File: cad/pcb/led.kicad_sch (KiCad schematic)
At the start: 0 parts

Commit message: finish overview schematic page
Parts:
- added IC?: PI4IOE5V96224ZLEX, QFN40P300X600X80-33N, symbol PI4IOE5V96224ZLEX:PI4IOE5V96224ZLEX
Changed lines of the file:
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@@
     (comment 4 "Simon Brenninger")
   )
+  (symbol (lib_id "PI4IOE5V96224ZLEX:PI4IOE5V96224ZLEX") (at 59.69 52.07 0) (unit 1)
+    (in_bom yes) (on_board yes) (fields_autoplaced)
+    (property "Reference" "IC?" (id 0) (at 82.0294 92.71 0)
+      (effects (font (size 1.27 1.27)) (justify left))
+    )
+    (property "Value" "PI4IOE5V96224ZLEX" (id 1) (at 82.0294 95.25 0)
+      (effects (font (size 1.27 1.27)) (justify left))
+    )
+    (property "Footprint" "QFN40P300X600X80-33N" (id 2) (at 88.9 41.91 0)
+      (effects (font (size 1.27 1.27)) (justify left) hide)
+    )
+    (property "Datasheet" "https://www.diodes.com/assets/Datasheets/PI4IOE5V96224.pdf" (id 3) (at 88.9 44.45 0)
+      (effects (font (size 1.27 1.27)) (justify left) hide)
+    )
+    (property "Description" "Interface - I/O Expanders 24-bit I2C-bus I/O Expander" (id 4) (at 88.9 46.99 0)
+      (effects (font (size 1.27 1.27)) (justify left) hide)
+    )
+    (property "Height" "0.8" (id 5) (at 88.9 49.53 0)
+      (effects (font (size 1.27 1.27)) (justify left) hide)
+    )
+    (property "Mouser Part Number" "729-I4IOE5V96224ZLEX" (id 6) (at 88.9 52.07 0)
+      (effects (font (size 1.27 1.27)) (justify left) hide)
+    )
+    (property "Mouser Price/Stock" "https://www.mouser.co.uk/ProductDetail/Diodes-Incorporated/PI4IOE5V96224ZLEX?qs=0lQeLiL1qybZKU%252B6WN8aKg%3D%3D" (id 7) (at 88.9 54.61 0)
+      (effects (font (size 1.27 1.27)) (justify left) hide)
+    )
+    (property "Manufacturer_Name" "Diodes Inc." (id 8) (at 88.9 57.15 0)
+      (effects (font (size 1.27 1.27)) (justify left) hide)
+    )
+    (property "Manufacturer_Part_Number" "PI4IOE5V96224ZLEX" (id 9) (at 88.9 59.69 0)
+      (effects (font (size 1.27 1.27)) (justify left) hide)
+    )
+    (pin "1")
+    (pin "10")
+    (pin "11")
+    (pin "12")
+    (pin "13")
+    (pin "14")
+    (pin "15")
+    (pin "16")
+    (pin "17")
+    (pin "18")
+    (pin "19")
+    (pin "2")
+    (pin "20")
+    (pin "21")
+    (pin "22")
+    (pin "23")
+    (pin "24")
+    (pin "25")
+    (pin "26")
+    (pin "27")
+    (pin "28")
+    (pin "29")
+    (pin "3")
+    (pin "30")
+    (pin "31")
+    (pin "32")
+    (pin "33")
+    (pin "4")
+    (pin "5")
+    (pin "6")
+    (pin "7")
+    (pin "8")
+    (pin "9")
+  )
 )

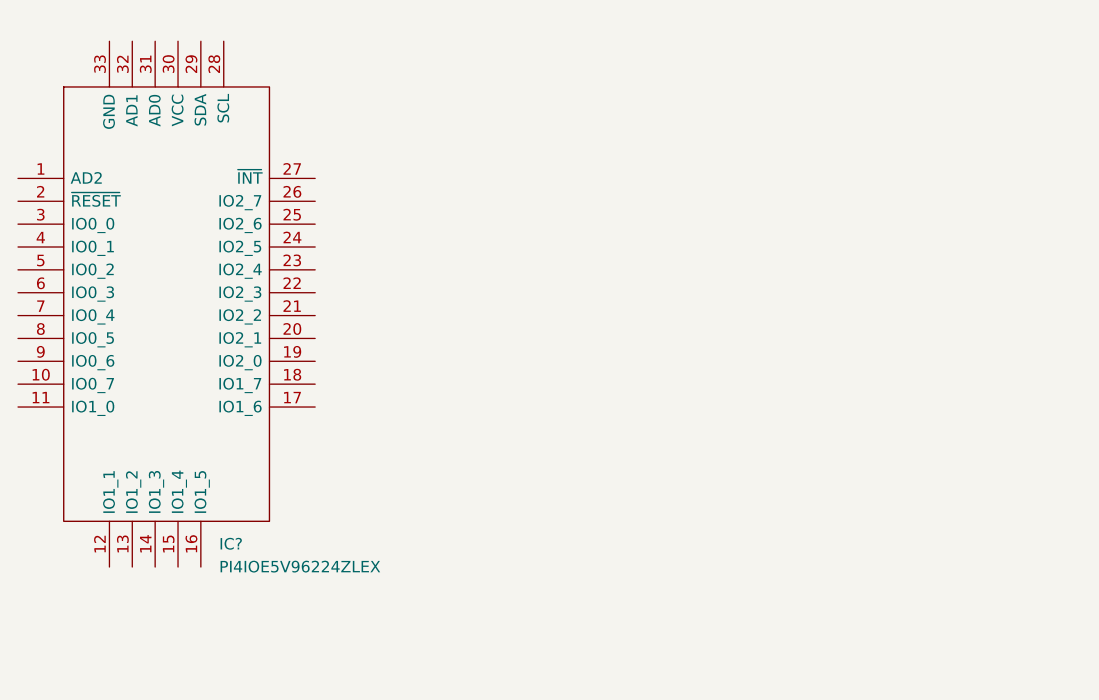
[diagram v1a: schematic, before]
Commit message: finish mcu connections
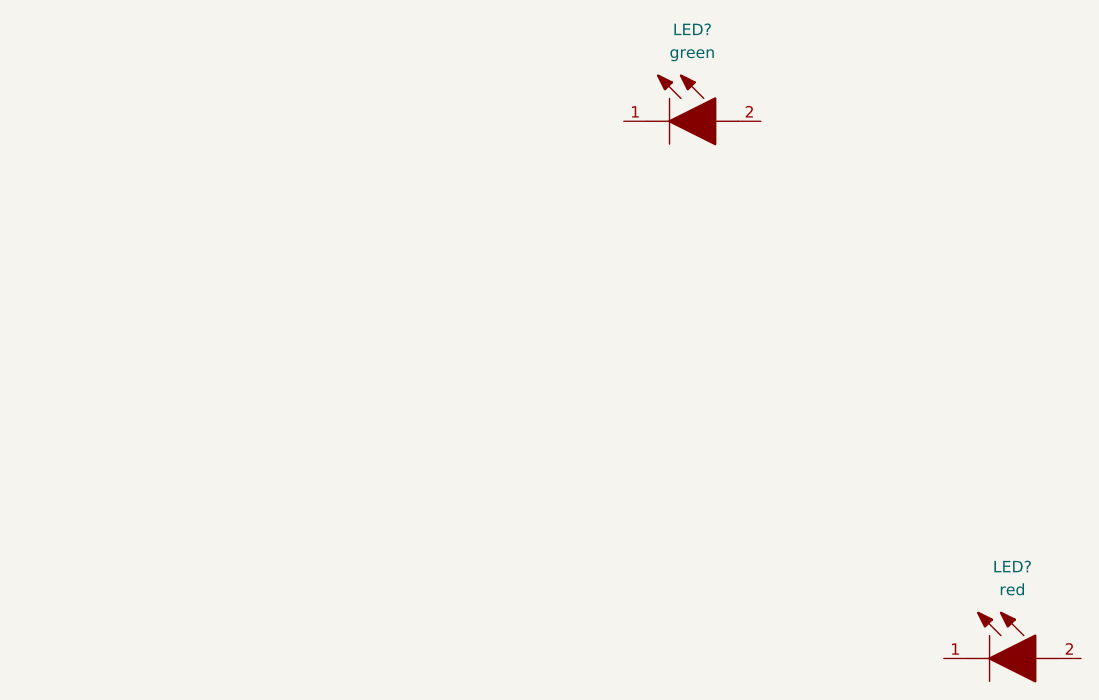
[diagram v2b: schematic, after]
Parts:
- removed IC?: PI4IOE5V96224ZLEX, QFN40P300X600X80-33N, symbol PI4IOE5V96224ZLEX:PI4IOE5V96224ZLEX
- added LED?: red, LEDC1608X80N, symbol LED red:150060SS75000
- added LED?: green, LEDM2012X80N, symbol LED green:150080GS75000
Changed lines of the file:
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@@
     (comment 4 "Simon Brenninger")
   )
-  (symbol (lib_id "PI4IOE5V96224ZLEX:PI4IOE5V96224ZLEX") (at 59.69 52.07 0) (unit 1)
+  (symbol (lib_id "LED red:150060SS75000") (at 162.56 105.41 0) (unit 1)
     (in_bom yes) (on_board yes) (fields_autoplaced)
-    (property "Reference" "IC?" (id 0) (at 82.0294 92.71 0)
-      (effects (font (size 1.27 1.27)) (justify left))
+    (property "Reference" "LED?" (id 0) (at 170.18 95.25 0))
+    (property "Value" "red" (id 1) (at 170.18 97.79 0))
+    (property "Footprint" "LEDC1608X80N" (id 2) (at 175.26 101.6 0)
+      (effects (font (size 1.27 1.27)) (justify left bottom) hide)
     )
-    (property "Value" "PI4IOE5V96224ZLEX" (id 1) (at 82.0294 95.25 0)
-      (effects (font (size 1.27 1.27)) (justify left))
+    (property "Datasheet" "" (id 3) (at 175.26 104.14 0)
+      (effects (font (size 1.27 1.27)) (justify left bottom) hide)
     )
-    (property "Footprint" "QFN40P300X600X80-33N" (id 2) (at 88.9 41.91 0)
-      (effects (font (size 1.27 1.27)) (justify left) hide)
+    (property "Description" "LED,Wurth Elektronik,150060SS75000 Wurth Elektronik 150060SS75000, WL-SMCW Series Red LED, 630 nm, 1608 (0603) Clear, Rectangle Lens SMD Package" (id 4) (at 175.26 106.68 0)
+      (effects (font (size 1.27 1.27)) (justify left bottom) hide)
     )
-    (property "Datasheet" "https://www.diodes.com/assets/Datasheets/PI4IOE5V96224.pdf" (id 3) (at 88.9 44.45 0)
-      (effects (font (size 1.27 1.27)) (justify left) hide)
+    (property "Height" "0.8" (id 5) (at 175.26 109.22 0)
+      (effects (font (size 1.27 1.27)) (justify left bottom) hide)
     )
-    (property "Description" "Interface - I/O Expanders 24-bit I2C-bus I/O Expander" (id 4) (at 88.9 46.99 0)
-      (effects (font (size 1.27 1.27)) (justify left) hide)
+    (property "Mouser Part Number" "710-150060SS75000" (id 6) (at 175.26 111.76 0)
+      (effects (font (size 1.27 1.27)) (justify left bottom) hide)
     )
-    (property "Height" "0.8" (id 5) (at 88.9 49.53 0)
-      (effects (font (size 1.27 1.27)) (justify left) hide)
+    (property "Mouser Price/Stock" "https://www.mouser.co.uk/ProductDetail/Wurth-Elektronik/150060SS75000?qs=LlUlMxKIyB0oQaxwspeTEA%3D%3D" (id 7) (at 175.26 114.3 0)
+      (effects (font (size 1.27 1.27)) (justify left bottom) hide)
     )
-    (property "Mouser Part Number" "729-I4IOE5V96224ZLEX" (id 6) (at 88.9 52.07 0)
-      (effects (font (size 1.27 1.27)) (justify left) hide)
+    (property "Manufacturer_Name" "Wurth Elektronik" (id 8) (at 175.26 116.84 0)
+      (effects (font (size 1.27 1.27)) (justify left bottom) hide)
     )
-    (property "Mouser Price/Stock" "https://www.mouser.co.uk/ProductDetail/Diodes-Incorporated/PI4IOE5V96224ZLEX?qs=0lQeLiL1qybZKU%252B6WN8aKg%3D%3D" (id 7) (at 88.9 54.61 0)
-      (effects (font (size 1.27 1.27)) (justify left) hide)
-    )
-    (property "Manufacturer_Name" "Diodes Inc." (id 8) (at 88.9 57.15 0)
-      (effects (font (size 1.27 1.27)) (justify left) hide)
-    )
-    (property "Manufacturer_Part_Number" "PI4IOE5V96224ZLEX" (id 9) (at 88.9 59.69 0)
-      (effects (font (size 1.27 1.27)) (justify left) hide)
+    (property "Manufacturer_Part_Number" "150060SS75000" (id 9) (at 175.26 119.38 0)
+      (effects (font (size 1.27 1.27)) (justify left bottom) hide)
     )
     (pin "1")
-    (pin "10")
-    (pin "11")
-    (pin "12")
-    (pin "13")
-    (pin "14")
-    (pin "15")
-    (pin "16")
-    (pin "17")
-    (pin "18")
-    (pin "19")
     (pin "2")
-    (pin "20")
-    (pin "21")
-    (pin "22")
-    (pin "23")
-    (pin "24")
-    (pin "25")
-    (pin "26")
-    (pin "27")
-    (pin "28")
-    (pin "29")
-    (pin "3")
-    (pin "30")
-    (pin "31")
-    (pin "32")
-    (pin "33")
-    (pin "4")
-    (pin "5")
-    (pin "6")
-    (pin "7")
-    (pin "8")
-    (pin "9")
+  )
+  (symbol (lib_id "LED green:150080GS75000") (at 127 45.72 0) (unit 1)
+    (in_bom yes) (on_board yes) (fields_autoplaced)
+    (property "Reference" "LED?" (id 0) (at 134.62 35.56 0))
+    (property "Value" "green" (id 1) (at 134.62 38.1 0))
+    (property "Footprint" "LEDM2012X80N" (id 2) (at 139.7 41.91 0)
+      (effects (font (size 1.27 1.27)) (justify left bottom) hide)
+    )
+    (property "Datasheet" "https://katalog.we-online.com/led/datasheet/150080GS75000.pdf" (id 3) (at 139.7 44.45 0)
+      (effects (font (size 1.27 1.27)) (justify left bottom) hide)
+    )
+    (property "Description" "150080GS75000, Wurth Elektronik WL-SMCW 520 nm Green LED, 2012 (0805) Clear SMD package" (id 4) (at 139.7 46.99 0)
+      (effects (font (size 1.27 1.27)) (justify left bottom) hide)
+    )
+    (property "Height" "0.8" (id 5) (at 139.7 49.53 0)
+      (effects (font (size 1.27 1.27)) (justify left bottom) hide)
+    )
+    (property "Mouser Part Number" "710-150080GS75000" (id 6) (at 139.7 52.07 0)
+      (effects (font (size 1.27 1.27)) (justify left bottom) hide)
+    )
+    (property "Mouser Price/Stock" "https://www.mouser.co.uk/ProductDetail/Wurth-Elektronik/150080GS75000?qs=2kOmHSv6VfQRoTEZVk1mGA%3D%3D" (id 7) (at 139.7 54.61 0)
+      (effects (font (size 1.27 1.27)) (justify left bottom) hide)
+    )
+    (property "Manufacturer_Name" "Wurth Elektronik" (id 8) (at 139.7 57.15 0)
+      (effects (font (size 1.27 1.27)) (justify left bottom) hide)
+    )
+    (property "Manufacturer_Part_Number" "150080GS75000" (id 9) (at 139.7 59.69 0)
+      (effects (font (size 1.27 1.27)) (justify left bottom) hide)
+    )
+    (pin "1")
+    (pin "2")
   )
 )

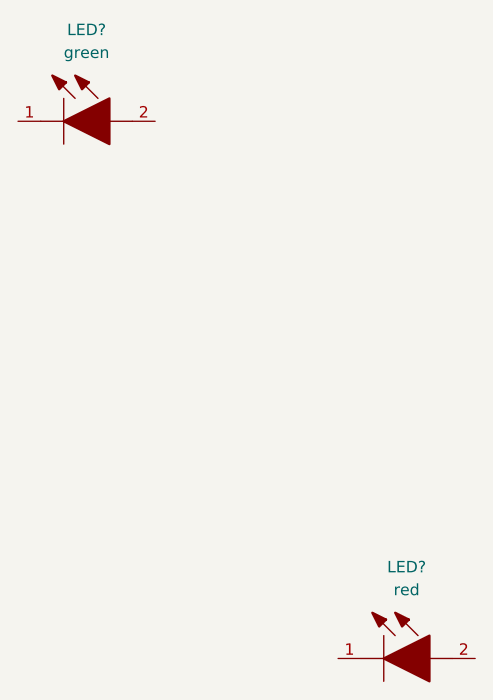
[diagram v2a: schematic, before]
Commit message: add charging & preotection circuit
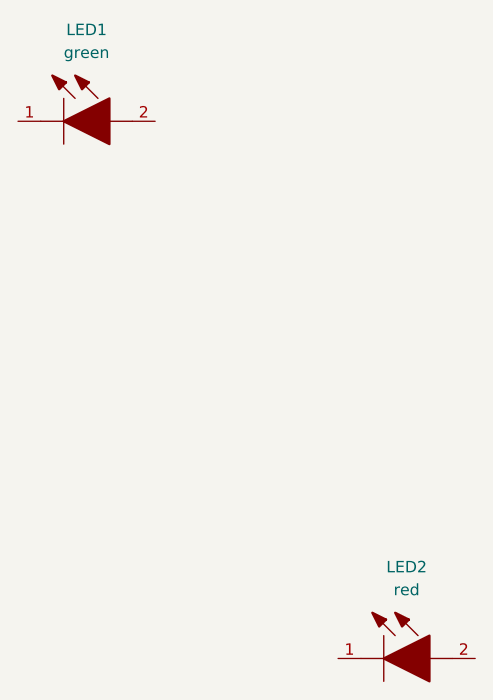
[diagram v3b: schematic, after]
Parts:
- gave numbers to parts that had none: 2
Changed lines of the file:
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@@
   (symbol (lib_id "LED red:150060SS75000") (at 162.56 105.41 0) (unit 1)
     (in_bom yes) (on_board yes) (fields_autoplaced)
-    (property "Reference" "LED?" (id 0) (at 170.18 95.25 0))
+    (property "Reference" "LED2" (id 0) (at 170.18 95.25 0))
     (property "Value" "red" (id 1) (at 170.18 97.79 0))
     (property "Footprint" "LEDC1608X80N" (id 2) (at 175.26 101.6 0)
@@
   (symbol (lib_id "LED green:150080GS75000") (at 127 45.72 0) (unit 1)
     (in_bom yes) (on_board yes) (fields_autoplaced)
-    (property "Reference" "LED?" (id 0) (at 134.62 35.56 0))
+    (property "Reference" "LED1" (id 0) (at 134.62 35.56 0))
     (property "Value" "green" (id 1) (at 134.62 38.1 0))
     (property "Footprint" "LEDM2012X80N" (id 2) (at 139.7 41.91 0)

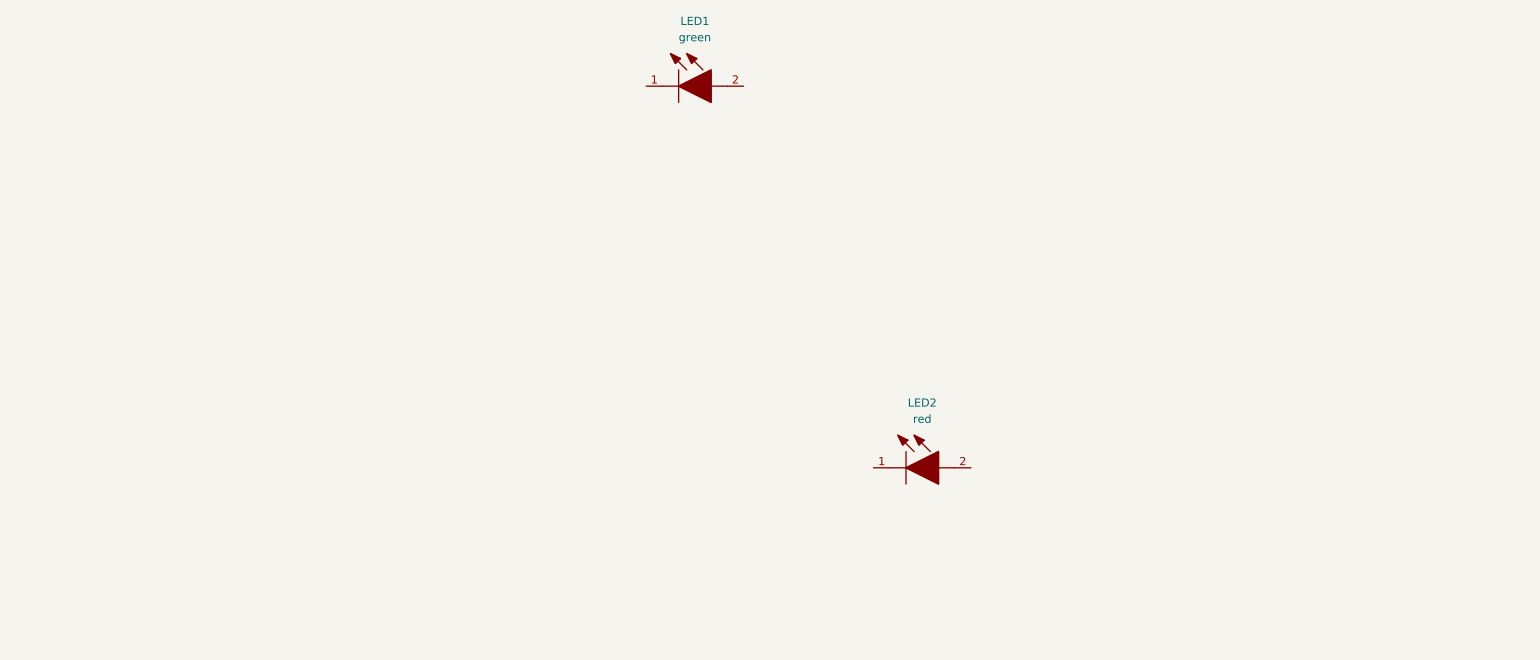
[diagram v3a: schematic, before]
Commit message: add LEDs for LED ring
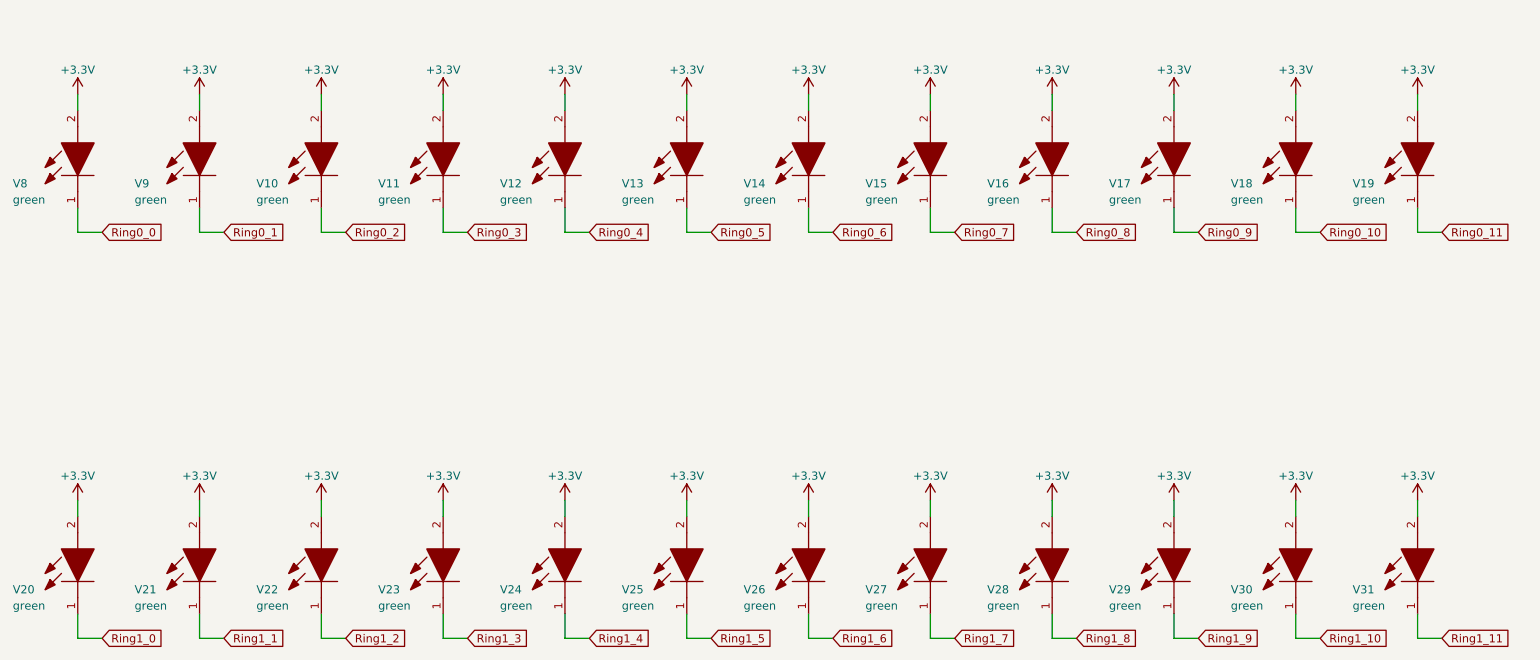
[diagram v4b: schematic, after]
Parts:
- removed LED2: red, LEDC1608X80N, symbol LED red:150060SS75000
- added V10, V11, V12, V13, V14, V15, V16, V17, V18, V19, V20, V21, V22, V23, V24, V25, V26, V27, V28, V29, V30, V31, V9: green, LED green:LEDM2012X80N, symbol LED green:150080GS75000
- V8: renamed from LED1; footprint LEDM2012X80N -> LED green:LEDM2012X80N
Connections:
- net Ring0_0: now reaches V8.1
- net +3.3V: now reaches V8.2
- net +3.3V: now also V10.2, V11.2, V12.2, V13.2, V14.2, V15.2, V16.2, V17.2, V18.2, V19.2, V20.2, V21.2, V22.2, V23.2, V24.2, V25.2, V26.2, V27.2, V28.2, V29.2, V30.2, V31.2, V9.2
- new net Ring0_1: V9.1
- new net Ring0_10: V18.1
- new net Ring0_11: V19.1
- new net Ring0_2: V10.1
- new net Ring0_3: V11.1
- new net Ring0_4: V12.1
- new net Ring0_5: V13.1
- new net Ring0_6: V14.1
- new net Ring0_7: V15.1
- new net Ring0_8: V16.1
- new net Ring0_9: V17.1
- new net Ring1_0: V20.1
- new net Ring1_1: V21.1
- new net Ring1_10: V30.1
- new net Ring1_11: V31.1
- new net Ring1_2: V22.1
- new net Ring1_3: V23.1
- new net Ring1_4: V24.1
- new net Ring1_5: V25.1
- new net Ring1_6: V26.1
- new net Ring1_7: V27.1
- new net Ring1_8: V28.1
- new net Ring1_9: V29.1
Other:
- moved on the sheet: V8
